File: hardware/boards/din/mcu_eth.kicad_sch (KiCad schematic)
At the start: 60 parts, among them J101 USB-C, J102 HR911105A, J103 EXP, SW101 TL3342, SW102 TL3342, U101 ESP32-S3-WROOM-1-N8R2, U102 USBLC6-2SC6, U103 AP2114H-3.3TRG1, U104 W5500, Y101 25MHz

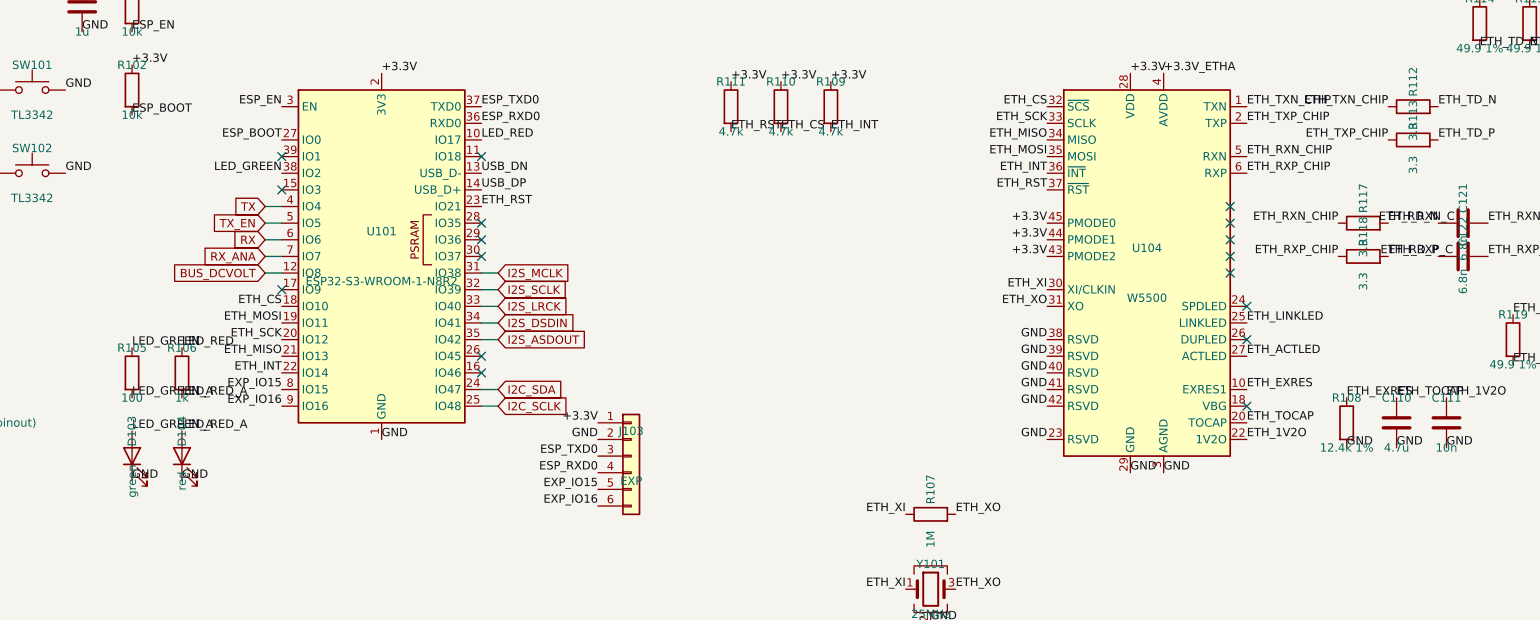
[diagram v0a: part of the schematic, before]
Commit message: gdoor-din: cut JLC Extended-part fees from $60 to $21
Hand-soldered and left off the JLC order (jlcfab.py HAND_SOLDERED): J1,
J102, U103, U102, U2/U3, C19/C20/C59, Y101.

No-fee parts instead of Extended ones (schematic, board fields, DESIGN.md):
- 18k, 2.4k, 6.8 nF: same values as Preferred parts C25762/C25882/C1542
- 82k -> 100k Basic C25741: R3/R4 and R18/R19 are 1:1 reference dividers;
  R35 makes the bus-voltage divider 100k/10k (/11, about 34 V full scale)
- R112/R113/R117/R118 3.3 ohm -> 0 ohm: series resistors between the W5500
  and its 49.9 ohm terminations
- D103 green -> red C2286, R105 100 ohm -> 1k so both LEDs run ~1.3 mA

Still Extended: U1, U5, U101, U104, J101, R1/R20 (130k), R108 (12.4k).
Also a root .gitignore for .vscode/.

Co-Authored-By: Claude Opus 5.5 <noreply@anthropic.com>
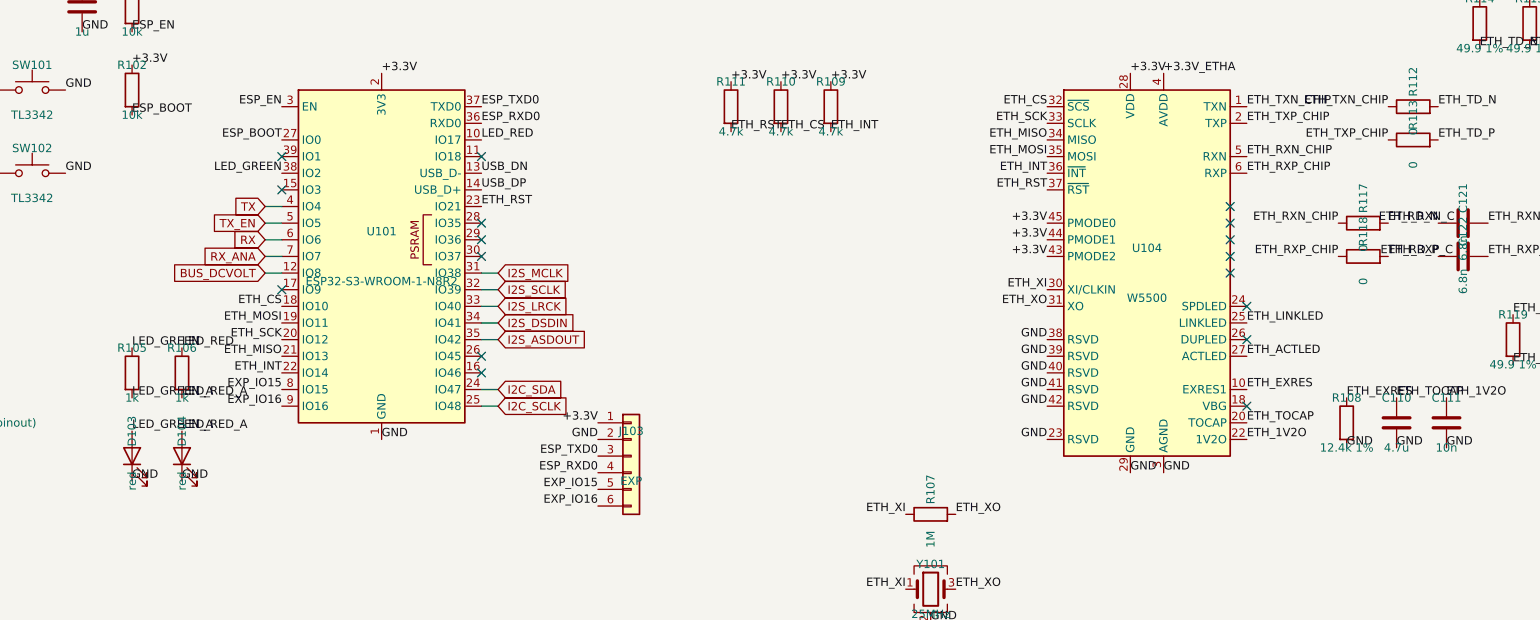
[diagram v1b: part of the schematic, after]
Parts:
- C121, C122: LCSC C93654 -> C1542
- D103: value green -> red; LCSC C12624 -> C2286
- R105: value 100 -> 1k; LCSC C25076 -> C11702
- R112, R113, R117, R118: value 3.3 -> 0; LCSC C2933094 -> C17168
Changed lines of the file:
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@@
 			)
 		)
-		(property "Value" "3.3"
+		(property "Value" "0"
 			(at 309.88 82.55 0)
 			(show_name no)
@@
 			)
 		)
-		(property "LCSC" "C2933094"
+		(property "LCSC" "C17168"
 			(at 0 0 0)
 			(hide yes)
@@
 			)
 		)
-		(property "Value" "3.3"
+		(property "Value" "0"
 			(at 302.26 100.33 0)
 			(show_name no)
@@
 			)
 		)
-		(property "LCSC" "C2933094"
+		(property "LCSC" "C17168"
 			(at 0 0 0)
 			(hide yes)
@@
 			)
 		)
-		(property "Value" "3.3"
+		(property "Value" "0"
 			(at 302.26 105.41 0)
 			(show_name no)
@@
 			)
 		)
-		(property "LCSC" "C2933094"
+		(property "LCSC" "C17168"
 			(at 0 0 0)
 			(hide yes)
@@
 			)
 		)
-		(property "LCSC" "C93654"
+		(property "LCSC" "C1542"
 			(at 0 0 0)
 			(hide yes)
@@
 			)
 		)
-		(property "LCSC" "C93654"
+		(property "LCSC" "C1542"
 			(at 0 0 0)
 			(hide yes)
@@
 			)
 		)
-		(property "Value" "green"
+		(property "Value" "red"
 			(at 114.3 135.89 0)
 			(show_name no)
@@
 			)
 		)
-		(property "LCSC" "C12624"
+		(property "LCSC" "C2286"
 			(at 0 0 0)
 			(hide yes)
@@
 			)
 		)
-		(property "Value" "100"
+		(property "Value" "1k"
 			(at 114.3 123.19 0)
 			(show_name no)
@@
 			)
 		)
-		(property "LCSC" "C25076"
+		(property "LCSC" "C11702"
 			(at 0 0 0)
 			(hide yes)
@@
 			)
 		)
-		(property "Value" "3.3"
+		(property "Value" "0"
 			(at 309.88 87.63 0)
 			(show_name no)
@@
 			)
 		)
-		(property "LCSC" "C2933094"
+		(property "LCSC" "C17168"
 			(at 0 0 0)
 			(hide yes)

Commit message: gdoor-din: crystal caps 18 pF -> 33 pF, Ethernet front-end simulation
Y101 (C164045) is rated for CL = 20 pF; C108/C109 at 18 pF gave only
12-14 pF with stray, pulling the 25 MHz clock +35..+55 ppm (802.3u
allows +-50 ppm). 33 pF (C1562, JLC Basic) keeps it within +-7 ppm.

Add spice/eth_sim.py: W5500 + HR911105A front end (magjack fitted to
typical 10/100 figures). Return loss passes 802.3 on both pairs (~3.5 dB
margin), ~40 mA TX current gives the nominal 1.0 V MLT-3 level, FB101
has no resonance problem, C121/C122 put the RX low corner at 220 kHz as
in WIZnet's reference. plot.py's svg_plot is now importable.

Production files regenerated (BOM change only; gerbers differ in
timestamps).

Co-Authored-By: Claude Opus 5.5 <noreply@anthropic.com>
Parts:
- C108, C109: value 18p -> 33p; LCSC C1549 -> C1562
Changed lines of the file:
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@@
 			)
 		)
-		(property "Value" "18p"
+		(property "Value" "33p"
 			(at 228.6 168.91 0)
 			(show_name no)
@@
 			)
 		)
-		(property "LCSC" "C1549"
+		(property "LCSC" "C1562"
 			(at 0 0 0)
 			(hide yes)
@@
 			)
 		)
-		(property "Value" "18p"
+		(property "Value" "33p"
 			(at 243.84 168.91 0)
 			(show_name no)
@@
 			)
 		)
-		(property "LCSC" "C1549"
+		(property "LCSC" "C1562"
 			(at 0 0 0)
 			(hide yes)

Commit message: gdoor-din: J103 gets LCSC C37208
J103 (1x6 2.54 mm expansion header) was the only part without an LCSC
number. C37208: BOOMELE 1x6P straight through-hole, gold. It is
hand-soldered (jlcfab.py HAND_SOLDERED), so the JLC BOM and CPL do not
change. The board field is hidden on F.Fab like the others.

Co-Authored-By: Claude Opus 5.5 <noreply@anthropic.com>
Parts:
- J103: LCSC (none) -> C37208
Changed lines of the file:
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@@
 			)
 		)
+    (property "LCSC" "C37208" (at 190.5 132.08 0)
+      (effects (font (size 1.27 1.27)) (hide yes))
+    )
 		(pin "4"
 		)

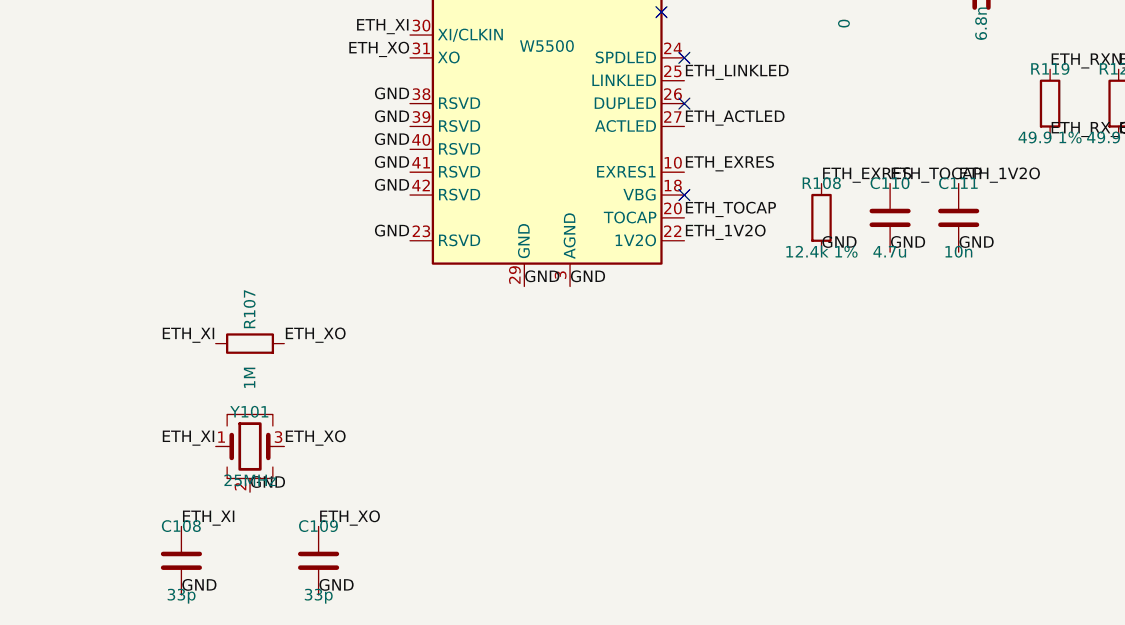
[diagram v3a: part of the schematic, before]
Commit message: gdoor-din: four JLC Extended parts made fee-free, values kept
Saves $12 of JLC's $3-per-type Extended loading fee (8 charged types -> 4).

- R3/R4 82k: 0402 C2909388 -> 0603 C23254 (Basic).
- R1/R20 130k: 0402 C2909318 -> 0603 C22795 (Preferred Extended).
  The larger pads needed two small reroutes: Net-(J1-Pin_2) between R3
  and R5, and the Net-(C8-Pad2) diagonal next to R20.
- R108 12.4k 1% (C2929935) -> R108 10k (C25744) + new R123 2.4k
  (C25882) in series, node ETH_EXRES_LO; 12.4k exactly. R123 sits below
  R108; the GND via beside R108 pad 2 moved to R123 pad 2.
- Y101 C164045 (CL 20 pF, +-50 ppm) -> C9006 (CL 12 pF, +-20 ppm, Basic),
  same 3225 footprint; C108/C109 33 pF -> 15 pF (C1548). eth_sim.py puts
  the pull at -5.5..+18.5 ppm, worst case ~+48.5 ppm with tolerance and
  temperature, inside 802.3u's +-50 ppm.

DRC (zone refill): 0 errors, 0 unconnected, schematic parity clean.
Production files regenerated with jlcfab.py. mcu_eth.kicad_sch was
rewritten in compact s-expression layout by the Konnect schematic tool;
a netlist comparison shows only the changes above.

Also contains an unrelated one-line change from another session: J101's
3D-model offset (y 0.294 -> -1.045) in esp32.kicad_pcb.

Co-Authored-By: Claude Opus 5.5 <noreply@anthropic.com>
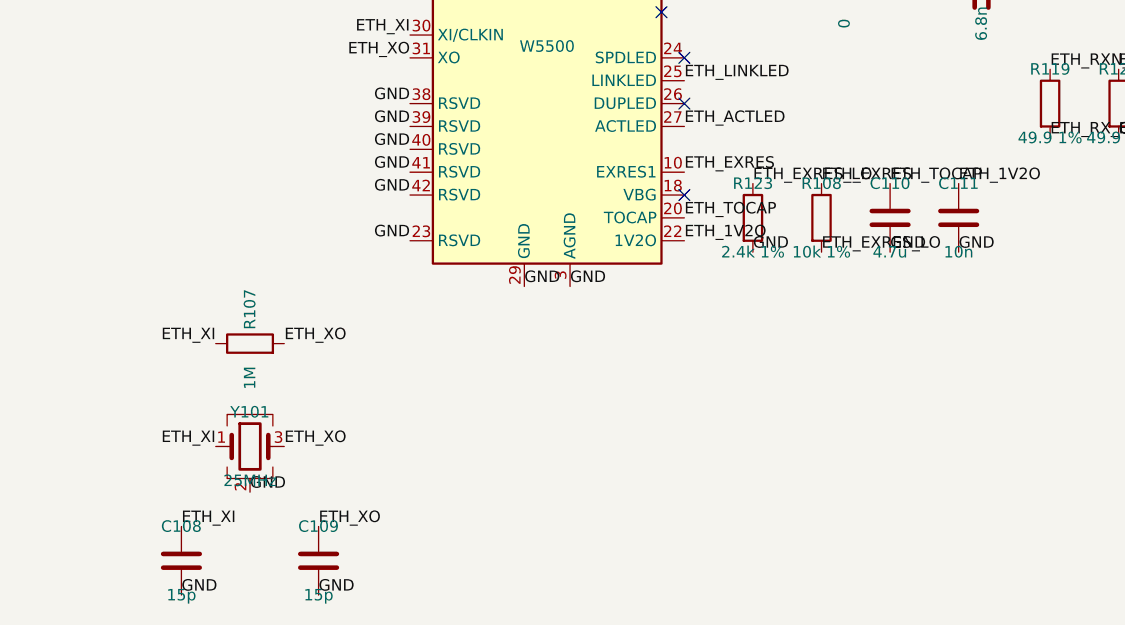
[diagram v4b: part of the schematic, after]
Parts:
- added R123: 2.4k 1%, Resistor_SMD:R_0402_1005Metric, symbol Device:R
- C108, C109: value 33p -> 15p; LCSC C1562 -> C1548
- R108: value 12.4k 1% -> 10k 1%; LCSC C2929935 -> C25744
- Y101: LCSC C164045 -> C9006
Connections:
- net GND: now also R123.2; no longer R108.2
- new net ETH_EXRES_LO: R108.2, R123.1

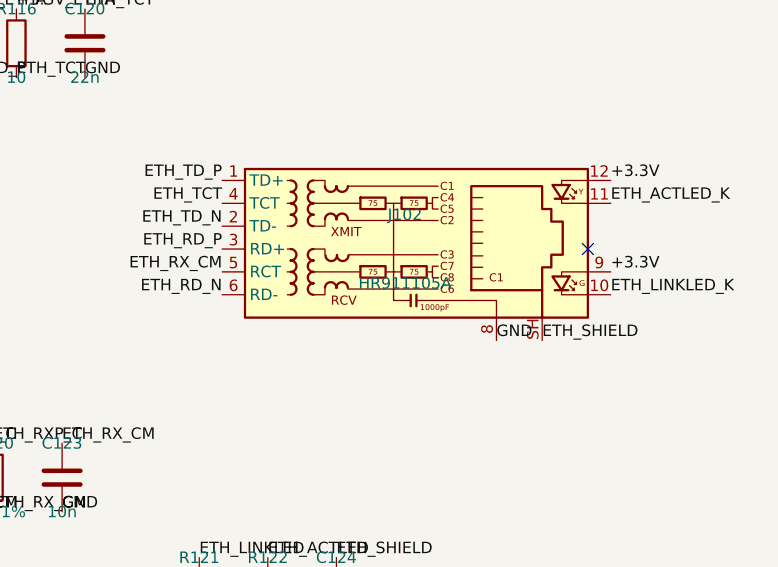
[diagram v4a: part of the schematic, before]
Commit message: gdoor-din: J102 to HanRun HY911105AE (C69427)
HR911105A (C12074) is out of stock at LCSC. HY911105AE is HanRun's
-40..+85 C version of the same jack: same pinout, LEDs, magnetics and
hole pattern, so the footprint stays. Updates the LCSC field, value and
datasheet, and the BOM, hand-solder and price files.

Co-Authored-By: Claude Opus 5.5 <noreply@anthropic.com>
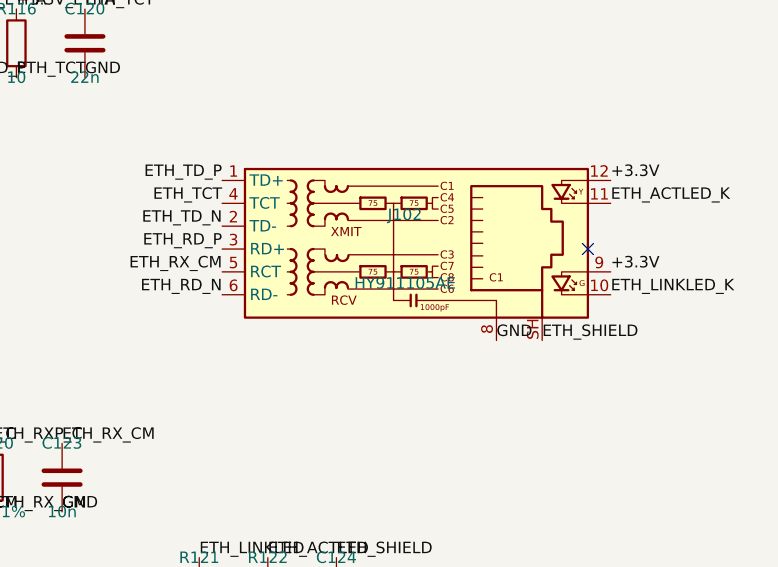
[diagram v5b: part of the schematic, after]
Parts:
- J102: value HR911105A -> HY911105AE; LCSC C12074 -> C69427
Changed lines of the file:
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@@
         (font
           (size 1.27 1.27))))
-    (property "Value" "HR911105A"
+    (property "Value" "HY911105AE"
       (at 378.46 92.71 0)
       (show_name no)
@@
         (font
           (size 1.27 1.27))))
-    (property "Datasheet" ""
+    (property "Datasheet" "https://www.lcsc.com/datasheet/C69427.pdf"
       (at 378.46 88.9 0)
       (hide yes)
@@
         (font
           (size 1.27 1.27))))
-    (property "LCSC" "C12074"
+    (property "LCSC" "C69427"
       (at 0 0 0)
       (hide yes)
